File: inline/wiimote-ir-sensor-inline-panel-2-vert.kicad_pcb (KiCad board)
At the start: 2 copper layers, 13 x 45 mm, 92 parts, among them J1 Conn_01x05_Pin, U2 AP2112-3.3V, X1 SG3225CAN 24.0000M-TJGA3

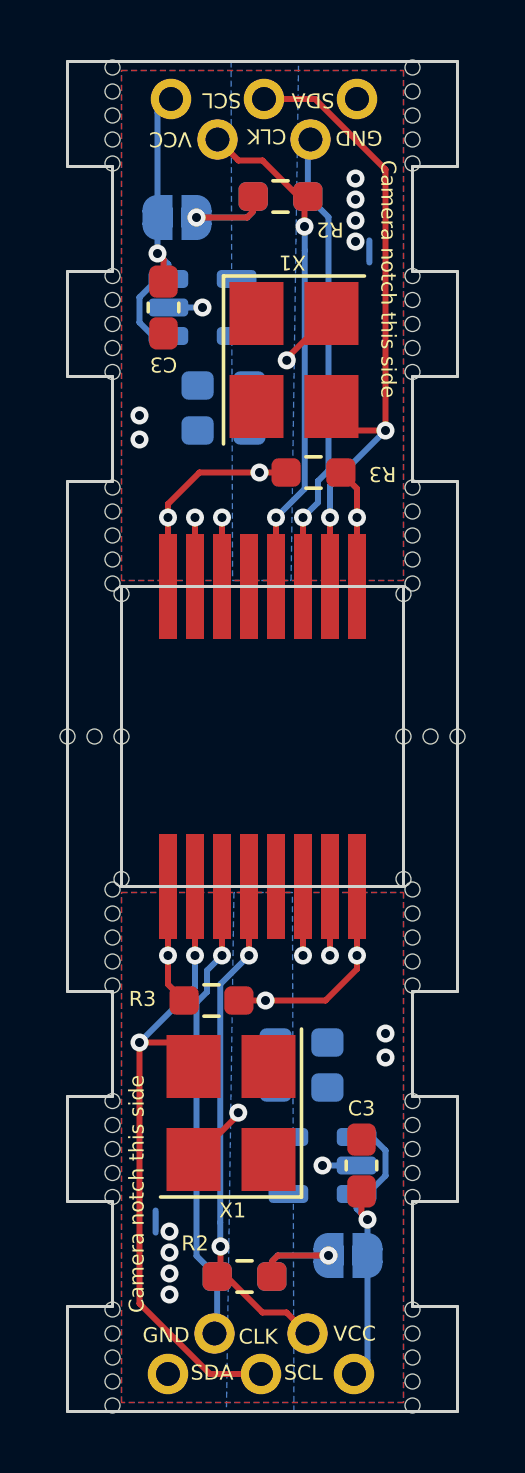
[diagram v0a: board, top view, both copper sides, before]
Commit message: Cheaper PCBA (#3)
* Move all components to one side of the board for cheaper PCBA

* Socketed: Add option to wire CLK directly
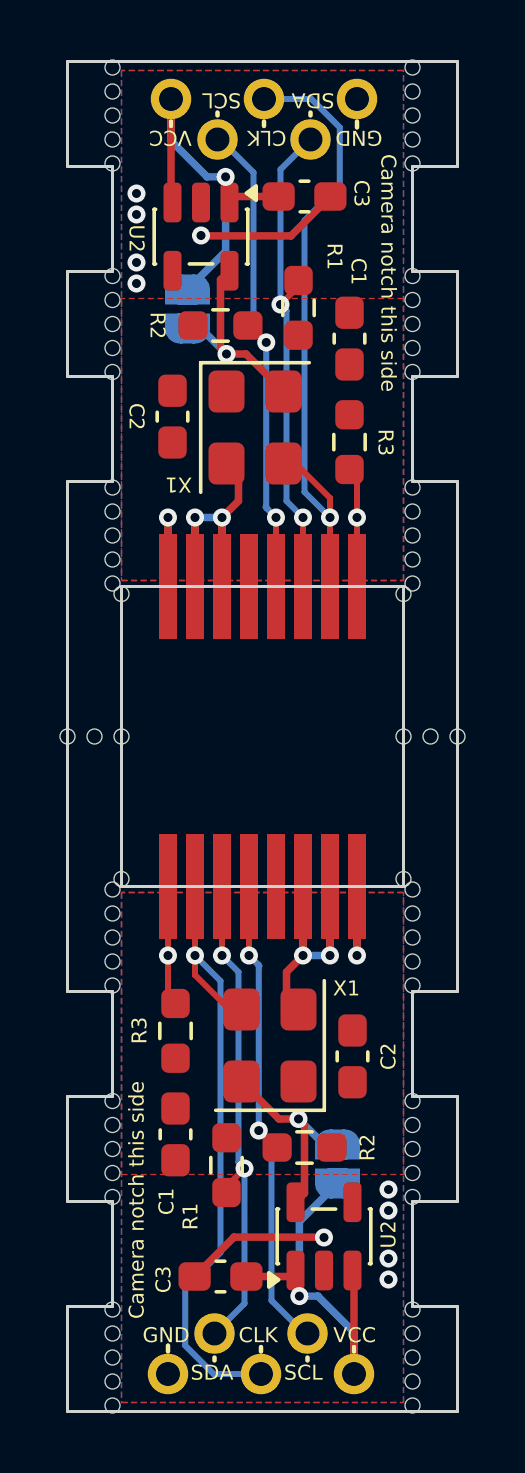
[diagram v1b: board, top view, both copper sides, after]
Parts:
- removed the C1 at (147.2, 32.3)
- removed the C1 at (149.8, 52.7)
- removed the C2 at (147.2, 30.8)
- removed the C2 at (149.8, 54.2)
- removed the C3 at (151.8, 56.8)
- removed the C3 at (145.2, 28.2)
- removed the JP1 at (145.7, 25.2)
- removed the JP1 at (151.3, 59.8)
- removed the R1 at (147.9, 60.5)
- removed the R1 at (149.1, 24.5)
- removed the R2 at (147.9, 60.5)
- removed the R2 at (149.1, 24.5)
- removed the R3 at (146.8, 51.3)
- removed the R3 at (150.2, 33.7)
- removed the REF** at (143.5, 48.4)
- removed the REF** at (143.5, 29.6)
- removed the REF** at (153.5, 64.0)
- removed the REF** at (153.5, 34.2)
- removed the REF** at (143.5, 62.4)
- removed the REF** at (143.5, 20.2)
- removed the REF** at (143.5, 49.2)
- removed the REF** at (153.5, 57.9)
- removed the REF** at (143.5, 36.6)
- removed the REF** at (153.5, 21.0)
- removed the REF** at (143.5, 27.9)
- removed the REF** at (153.5, 54.6)
- removed the REF** at (143.5, 57.0)
- removed the REF** at (153.2, 47.2)
- removed the REF** at (153.5, 37.4)
- removed the REF** at (143.5, 21.0)
- removed the REF** at (153.5, 35.0)
- removed the REF** at (143.5, 50.8)
- removed the REF** at (143.5, 50.0)
- removed the REF** at (153.5, 55.5)
- removed the REF** at (143.5, 23.4)
- removed the REF** at (153.5, 22.6)
- removed the REF** at (143.5, 21.8)
- removed the REF** at (153.2, 37.8)
- removed the REF** at (153.5, 30.4)
- removed the REF** at (143.8, 37.8)
- removed the REF** at (143.5, 56.2)
- removed the REF** at (143.5, 37.4)
- removed the REF** at (153.5, 20.2)
- removed the REF** at (153.5, 62.4)
- removed the REF** at (143.8, 47.2)
- removed the REF** at (153.5, 28.8)
- removed the REF** at (143.5, 55.5)
- removed the REF** at (143.5, 64.8)
- removed the REF** at (153.5, 21.8)
- removed the REF** at (143.5, 61.6)
- removed the REF** at (153.5, 29.6)
- removed the REF** at (143.5, 64.0)
- removed the REF** at (143.5, 34.2)
- removed the REF** at (153.5, 57.0)
- removed the REF** at (153.5, 27.9)
- removed the REF** at (143.5, 57.9)
- removed the REF** at (153.5, 64.8)
- removed the REF** at (143.5, 30.4)
- removed the REF** at (153.5, 61.6)
- removed the REF** at (143.5, 28.8)
- removed the REF** at (153.5, 50.0)
- removed the REF** at (143.5, 35.8)
- removed the REF** at (153.5, 35.8)
- removed the REF** at (153.5, 36.6)
- removed the REF** at (153.5, 49.2)
- removed the REF** at (153.5, 27.1)
- removed the REF** at (143.5, 35.0)
- removed the REF** at (153.5, 47.6)
- removed the REF** at (143.5, 63.2)
- removed the REF** at (153.5, 56.2)
- removed the REF** at (153.5, 23.4)
- removed the REF** at (153.5, 63.2)
- removed the REF** at (143.5, 22.6)
- removed the REF** at (143.5, 47.6)
- removed the REF** at (143.5, 27.1)
- removed the REF** at (143.5, 54.6)
- removed the REF** at (153.5, 48.4)
- removed the REF** at (153.5, 50.8)
- removed the U2 at (146.5, 28.2)
- removed the U2 at (150.5, 56.8)
- removed the X1 at (149.6, 29.9)
- removed the X1 at (147.4, 55.0)
- added C1: 0.1uF, Capacitor_SMD:C_0603_1608Metric_Pad1.08x0.95mm_HandSolder, F.Cu at (145.6, 55.8)
- added C1: 0.1uF, Capacitor_SMD:C_0603_1608Metric_Pad1.08x0.95mm_HandSolder, F.Cu at (151.4, 29.2)
- added C2: 1uF, Capacitor_SMD:C_0603_1608Metric_Pad1.08x0.95mm_HandSolder, F.Cu at (145.5, 31.8)
- added C2: 1uF, Capacitor_SMD:C_0603_1608Metric_Pad1.08x0.95mm_HandSolder, F.Cu at (151.5, 53.2)
- added C3: 1uF, Capacitor_SMD:C_0603_1608Metric_Pad1.08x0.95mm_HandSolder, F.Cu at (147.1, 60.5)
- added C3: 1uF, Capacitor_SMD:C_0603_1608Metric_Pad1.08x0.95mm_HandSolder, F.Cu at (149.9, 24.5)
- added JP1: SolderJumper_2_Open, Jumper:SolderJumper-2_P1.3mm_Open_RoundedPad1.0x1.5mm, B.Cu at (146.0, 28.2)
- added JP1: SolderJumper_2_Open, Jumper:SolderJumper-2_P1.3mm_Open_RoundedPad1.0x1.5mm, B.Cu at (151.0, 56.8)
- added R1: 2.7K, Resistor_SMD:R_0603_1608Metric_Pad0.98x0.95mm_HandSolder, F.Cu at (147.3, 56.8)
- added R1: 2.7K, Resistor_SMD:R_0603_1608Metric_Pad0.98x0.95mm_HandSolder, F.Cu at (149.7, 28.2)
- added R2: 2.7K, Resistor_SMD:R_0603_1608Metric_Pad0.98x0.95mm_HandSolder, F.Cu at (147.1, 28.8)
- added R2: 2.7K, Resistor_SMD:R_0603_1608Metric_Pad0.98x0.95mm_HandSolder, F.Cu at (149.9, 56.2)
- added R3: 33K, Resistor_SMD:R_0603_1608Metric_Pad0.98x0.95mm_HandSolder, F.Cu at (145.6, 52.3)
- added R3: 33K, Resistor_SMD:R_0603_1608Metric_Pad0.98x0.95mm_HandSolder, F.Cu at (151.4, 32.7)
- added REF**: NPTH-0.5mm, wiimote-ir-sensor:NPTH-0.5mm, F.Cu at (153.5, 34.2)
- added REF**: NPTH-0.5mm, wiimote-ir-sensor:NPTH-0.5mm, F.Cu at (143.5, 64.0)
- added REF**: NPTH-0.5mm, wiimote-ir-sensor:NPTH-0.5mm, F.Cu at (143.5, 23.4)
- added REF**: NPTH-0.5mm, wiimote-ir-sensor:NPTH-0.5mm, F.Cu at (143.5, 28.8)
- added REF**: NPTH-0.5mm, wiimote-ir-sensor:NPTH-0.5mm, F.Cu at (153.5, 49.2)
- added REF**: NPTH-0.5mm, wiimote-ir-sensor:NPTH-0.5mm, F.Cu at (153.2, 47.2)
- added REF**: NPTH-0.5mm, wiimote-ir-sensor:NPTH-0.5mm, F.Cu at (153.5, 27.9)
- added REF**: NPTH-0.5mm, wiimote-ir-sensor:NPTH-0.5mm, F.Cu at (143.5, 55.5)
- added REF**: NPTH-0.5mm, wiimote-ir-sensor:NPTH-0.5mm, F.Cu at (153.5, 36.6)
- added REF**: NPTH-0.5mm, wiimote-ir-sensor:NPTH-0.5mm, F.Cu at (143.8, 47.2)
- added REF**: NPTH-0.5mm, wiimote-ir-sensor:NPTH-0.5mm, F.Cu at (153.5, 21.0)
- added REF**: NPTH-0.5mm, wiimote-ir-sensor:NPTH-0.5mm, F.Cu at (153.5, 23.4)
- added REF**: NPTH-0.5mm, wiimote-ir-sensor:NPTH-0.5mm, F.Cu at (153.5, 47.6)
- added REF**: NPTH-0.5mm, wiimote-ir-sensor:NPTH-0.5mm, F.Cu at (153.5, 27.1)
- added REF**: NPTH-0.5mm, wiimote-ir-sensor:NPTH-0.5mm, F.Cu at (153.5, 37.4)
- added REF**: NPTH-0.5mm, wiimote-ir-sensor:NPTH-0.5mm, F.Cu at (143.5, 63.2)
- added REF**: NPTH-0.5mm, wiimote-ir-sensor:NPTH-0.5mm, F.Cu at (153.5, 30.4)
- added REF**: NPTH-0.5mm, wiimote-ir-sensor:NPTH-0.5mm, F.Cu at (153.5, 35.8)
- added REF**: NPTH-0.5mm, wiimote-ir-sensor:NPTH-0.5mm, F.Cu at (153.5, 22.6)
- added REF**: NPTH-0.5mm, wiimote-ir-sensor:NPTH-0.5mm, F.Cu at (153.5, 20.2)
- added REF**: NPTH-0.5mm, wiimote-ir-sensor:NPTH-0.5mm, F.Cu at (143.5, 30.4)
- added REF**: NPTH-0.5mm, wiimote-ir-sensor:NPTH-0.5mm, F.Cu at (143.5, 20.2)
- added REF**: NPTH-0.5mm, wiimote-ir-sensor:NPTH-0.5mm, F.Cu at (143.5, 47.6)
- added REF**: NPTH-0.5mm, wiimote-ir-sensor:NPTH-0.5mm, F.Cu at (143.5, 29.6)
- added REF**: NPTH-0.5mm, wiimote-ir-sensor:NPTH-0.5mm, F.Cu at (143.5, 27.1)
- added REF**: NPTH-0.5mm, wiimote-ir-sensor:NPTH-0.5mm, F.Cu at (143.5, 57.0)
- added REF**: NPTH-0.5mm, wiimote-ir-sensor:NPTH-0.5mm, F.Cu at (153.5, 57.0)
- added REF**: NPTH-0.5mm, wiimote-ir-sensor:NPTH-0.5mm, F.Cu at (143.5, 61.6)
- added REF**: NPTH-0.5mm, wiimote-ir-sensor:NPTH-0.5mm, F.Cu at (153.5, 28.8)
- added REF**: NPTH-0.5mm, wiimote-ir-sensor:NPTH-0.5mm, F.Cu at (153.5, 62.4)
- added REF**: NPTH-0.5mm, wiimote-ir-sensor:NPTH-0.5mm, F.Cu at (153.5, 50.0)
- added REF**: NPTH-0.5mm, wiimote-ir-sensor:NPTH-0.5mm, F.Cu at (143.5, 35.0)
- added REF**: NPTH-0.5mm, wiimote-ir-sensor:NPTH-0.5mm, F.Cu at (153.5, 54.6)
- added REF**: NPTH-0.5mm, wiimote-ir-sensor:NPTH-0.5mm, F.Cu at (153.5, 50.8)
- added REF**: NPTH-0.5mm, wiimote-ir-sensor:NPTH-0.5mm, F.Cu at (143.5, 27.9)
- added REF**: NPTH-0.5mm, wiimote-ir-sensor:NPTH-0.5mm, F.Cu at (143.5, 21.0)
- added REF**: NPTH-0.5mm, wiimote-ir-sensor:NPTH-0.5mm, F.Cu at (143.5, 49.2)
- added REF**: NPTH-0.5mm, wiimote-ir-sensor:NPTH-0.5mm, F.Cu at (153.5, 56.2)
- added REF**: NPTH-0.5mm, wiimote-ir-sensor:NPTH-0.5mm, F.Cu at (143.5, 50.0)
- added REF**: NPTH-0.5mm, wiimote-ir-sensor:NPTH-0.5mm, F.Cu at (153.5, 35.0)
- added REF**: NPTH-0.5mm, wiimote-ir-sensor:NPTH-0.5mm, F.Cu at (153.5, 63.2)
- added REF**: NPTH-0.5mm, wiimote-ir-sensor:NPTH-0.5mm, F.Cu at (143.5, 21.8)
- added REF**: NPTH-0.5mm, wiimote-ir-sensor:NPTH-0.5mm, F.Cu at (153.5, 48.4)
- added REF**: NPTH-0.5mm, wiimote-ir-sensor:NPTH-0.5mm, F.Cu at (143.5, 36.6)
- added REF**: NPTH-0.5mm, wiimote-ir-sensor:NPTH-0.5mm, F.Cu at (143.5, 22.6)
- added REF**: NPTH-0.5mm, wiimote-ir-sensor:NPTH-0.5mm, F.Cu at (153.5, 55.5)
- added REF**: NPTH-0.5mm, wiimote-ir-sensor:NPTH-0.5mm, F.Cu at (153.5, 64.8)
- added REF**: NPTH-0.5mm, wiimote-ir-sensor:NPTH-0.5mm, F.Cu at (153.5, 21.8)
- added REF**: NPTH-0.5mm, wiimote-ir-sensor:NPTH-0.5mm, F.Cu at (153.5, 57.9)
- added REF**: NPTH-0.5mm, wiimote-ir-sensor:NPTH-0.5mm, F.Cu at (153.2, 37.8)
- added REF**: NPTH-0.5mm, wiimote-ir-sensor:NPTH-0.5mm, F.Cu at (143.5, 50.8)
- added REF**: NPTH-0.5mm, wiimote-ir-sensor:NPTH-0.5mm, F.Cu at (143.5, 64.8)
- added REF**: NPTH-0.5mm, wiimote-ir-sensor:NPTH-0.5mm, F.Cu at (143.5, 35.8)
- added REF**: NPTH-0.5mm, wiimote-ir-sensor:NPTH-0.5mm, F.Cu at (143.5, 54.6)
- added REF**: NPTH-0.5mm, wiimote-ir-sensor:NPTH-0.5mm, F.Cu at (143.5, 48.4)
- added REF**: NPTH-0.5mm, wiimote-ir-sensor:NPTH-0.5mm, F.Cu at (153.5, 64.0)
- added REF**: NPTH-0.5mm, wiimote-ir-sensor:NPTH-0.5mm, F.Cu at (153.5, 29.6)
- added REF**: NPTH-0.5mm, wiimote-ir-sensor:NPTH-0.5mm, F.Cu at (143.5, 56.2)
- added REF**: NPTH-0.5mm, wiimote-ir-sensor:NPTH-0.5mm, F.Cu at (143.5, 37.4)
- added REF**: NPTH-0.5mm, wiimote-ir-sensor:NPTH-0.5mm, F.Cu at (143.8, 37.8)
- added REF**: NPTH-0.5mm, wiimote-ir-sensor:NPTH-0.5mm, F.Cu at (143.5, 34.2)
- added REF**: NPTH-0.5mm, wiimote-ir-sensor:NPTH-0.5mm, F.Cu at (143.5, 57.9)
- added REF**: NPTH-0.5mm, wiimote-ir-sensor:NPTH-0.5mm, F.Cu at (143.5, 62.4)
- added REF**: NPTH-0.5mm, wiimote-ir-sensor:NPTH-0.5mm, F.Cu at (153.5, 61.6)
- added U2: AP2112-3.3V, Package_TO_SOT_SMD:SOT-23-5, F.Cu at (146.4, 25.8)
- added U2: AP2112-3.3V, Package_TO_SOT_SMD:SOT-23-5, F.Cu at (150.6, 59.2)
- added X1: SG3225CAN 24.0000M-TJGA3, Oscillator:Oscillator_SMD_SeikoEpson_SG8002CE-4Pin_3.2x2.5mm, F.Cu at (148.8, 52.8)
- added X1: SG3225CAN 24.0000M-TJGA3, Oscillator:Oscillator_SMD_SeikoEpson_SG8002CE-4Pin_3.2x2.5mm, F.Cu at (148.2, 32.2)
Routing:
- net Board_1-+3.3V: track 15.5 -> 10.8 mm, vias 4 -> 2
- net Board_0-+3.3V: track 15.5 -> 10.8 mm, vias 4 -> 2
- net Board_1-GND: track 11.1 -> 15.1 mm, vias 9 -> 7
- net Board_0-GND: track 11.1 -> 15.1 mm, vias 9 -> 7
- net Board_1-VCC: track 10.6 -> 13.7 mm
- net Board_0-VCC: track 10.6 -> 13.7 mm
- net Board_0-/CLK: track 24.1 -> 22.6 mm, vias 2 -> 1
- net Board_1-/CLK: track 24.1 -> 22.6 mm, vias 2 -> 1
- net Board_1-Net-(U1-RESET): track 6.32 -> 4.95 mm
- net Board_0-Net-(U1-RESET): track 6.32 -> 4.95 mm
- net Board_0-/SCL: track 19.5 -> 18.3 mm
- net Board_1-/SCL: track 19.5 -> 18.3 mm
- net Board_1-/SDA: track 17.9 -> 17.8 mm, vias 1 -> 2
- net Board_0-/SDA: track 17.9 -> 17.8 mm, vias 1 -> 2
- added copper zone on F.Cu, net Board_0-+3.3V
- added copper zone on F.Cu, net Board_1-+3.3V
- removed copper zone on B.Cu, net Board_0-+3.3V
- removed copper zone on B.Cu, net Board_1-+3.3V
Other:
- outline, holes or cut-outs redrawn
